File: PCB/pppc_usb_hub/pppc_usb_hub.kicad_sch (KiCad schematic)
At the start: 81 parts, among them J1 USB_C_Signal, J2 USB_C_Signal, J3 USB_A_1, J4 USB_A_2, J5 USB_A_3, J6 Con_Relay, J7 Conn_UART, J8 Conn_Debug, K1 Relay, Q1 DMG2305UX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

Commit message: Rev 2
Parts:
- C1, C10, C11, C15, C16, C17, C18, C19, C2, C20, C23, C24, C25, C3, C4, C5, C6, C7, C8, C9: footprint Capacitor_SMD:C_0201_0603Metric -> Capacitor_SMD:C_0603_1608Metric
- D2, D3, D4, D5, D6: footprint LED_SMD:LED_0201_0603Metric -> LED_SMD:LED_0603_1608Metric
- R1, R10, R11, R12, R13, R14, R15, R16, R17, R18, R19, R2, R20, R21, R22, R3, R4, R5, R6, R7, R8, R9: footprint Resistor_SMD:R_0201_0603Metric -> Resistor_SMD:R_0603_1608Metric
- SW4: footprint PCBLIB_SW-SMD_L6.0-W3.3-LS8.0_2024-05-19:SW-SMD_L6.0-W3.3-LS8.0 -> PCBLIB_SW-SMD_GT-TC020B-H035-L05_2024-05-21:SW-SMD_GT-TC020B-H035-L05
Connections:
- net DN1: now also U4.13 (DM4); no longer U4.3 (DM1)
- net DN2: now also U4.15 (DM3); no longer U4.13 (DM4)
- net DN3: now also U4.1 (DM2); no longer U4.15 (DM3)
- net DP1: now also U4.14 (DP4); no longer U4.4 (DP1)
- net DP2: now also U4.16 (DP3); no longer U4.14 (DP4)
- net DP3: now also U4.2 (DP2); no longer U4.16 (DP3)
- net MCU_DN: now also U4.3 (DM1); no longer U4.1 (DM2)
- net MCU_DP: now also U4.4 (DP1); no longer U4.2 (DP2)

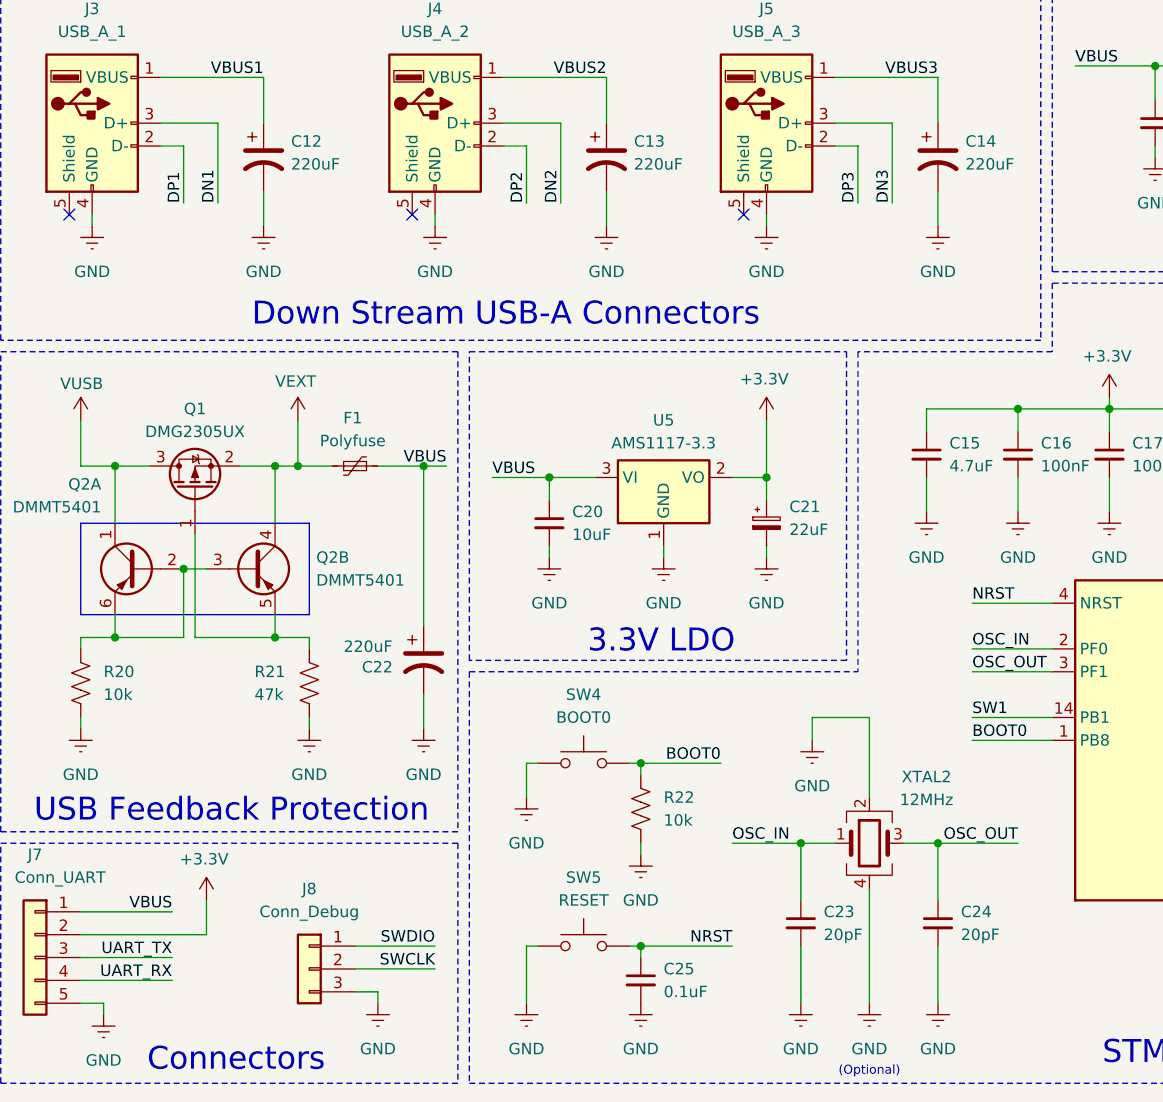
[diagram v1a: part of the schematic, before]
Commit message: Add firmware and update PCB to Rev 3
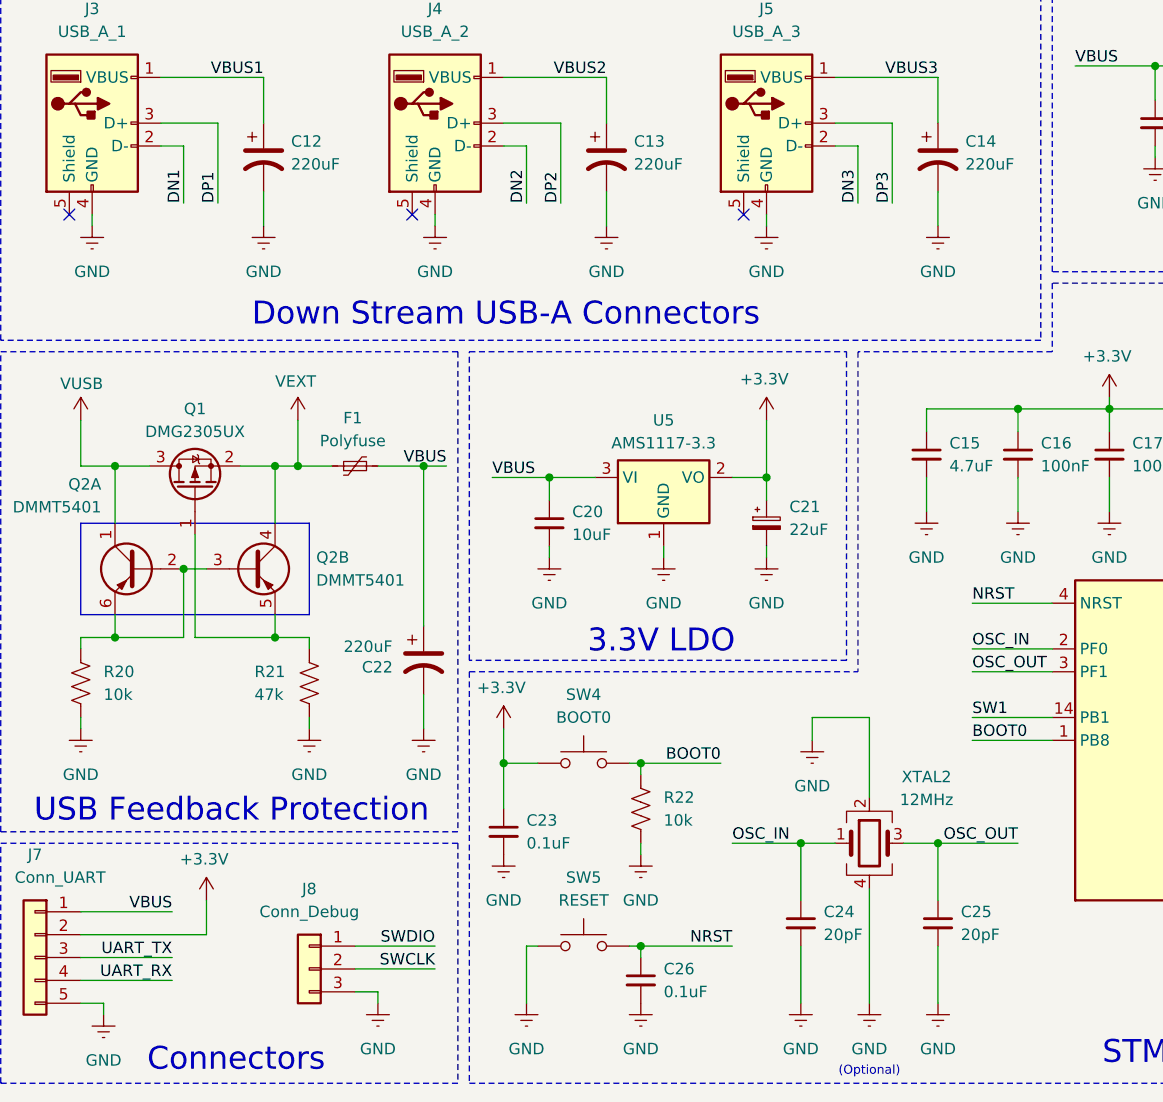
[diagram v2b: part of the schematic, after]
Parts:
- added C23: 0.1uF, Capacitor_SMD:C_0603_1608Metric, symbol Device:C_Small
- renumbered C23 to C24, C24 to C25, C25 to C26
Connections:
- net +3.3V: now also SW4.2, C23.1
- net DN1: now also J3.2 (D-); no longer J3.3 (D+)
- net DN2: now also J4.2 (D-); no longer J4.3 (D+)
- net DN3: now also J5.2 (D-); no longer J5.3 (D+)
- net DP1: now also J3.3 (D+); no longer J3.2 (D-)
- net DP2: now also J4.3 (D+); no longer J4.2 (D-)
- net DP3: now also J5.3 (D+); no longer J5.2 (D-)
- net GND: now also C23.2; no longer SW4.2
